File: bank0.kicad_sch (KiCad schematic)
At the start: 2 parts, among them U2 W25Q256FVEI, U201 xc7z010clg400

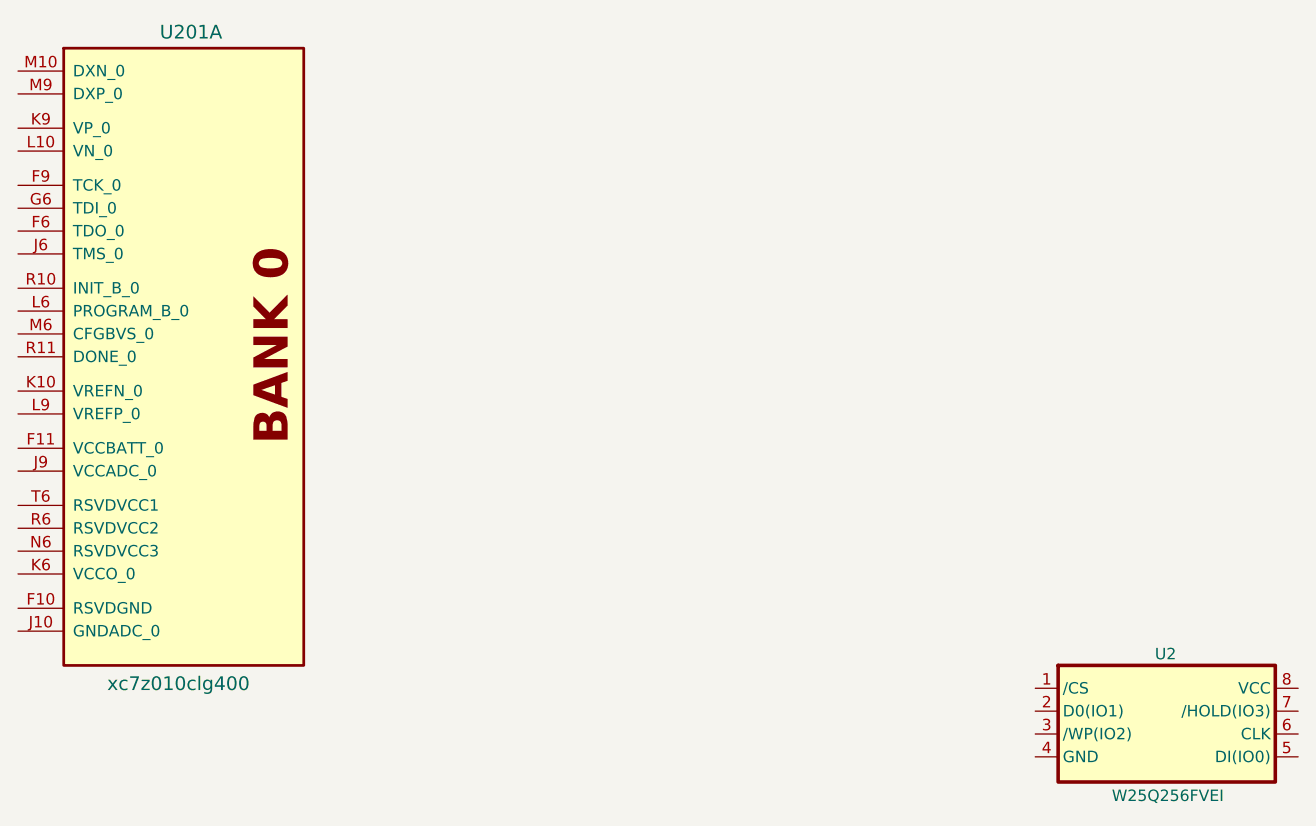
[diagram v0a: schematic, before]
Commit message: feat: finish power sch design
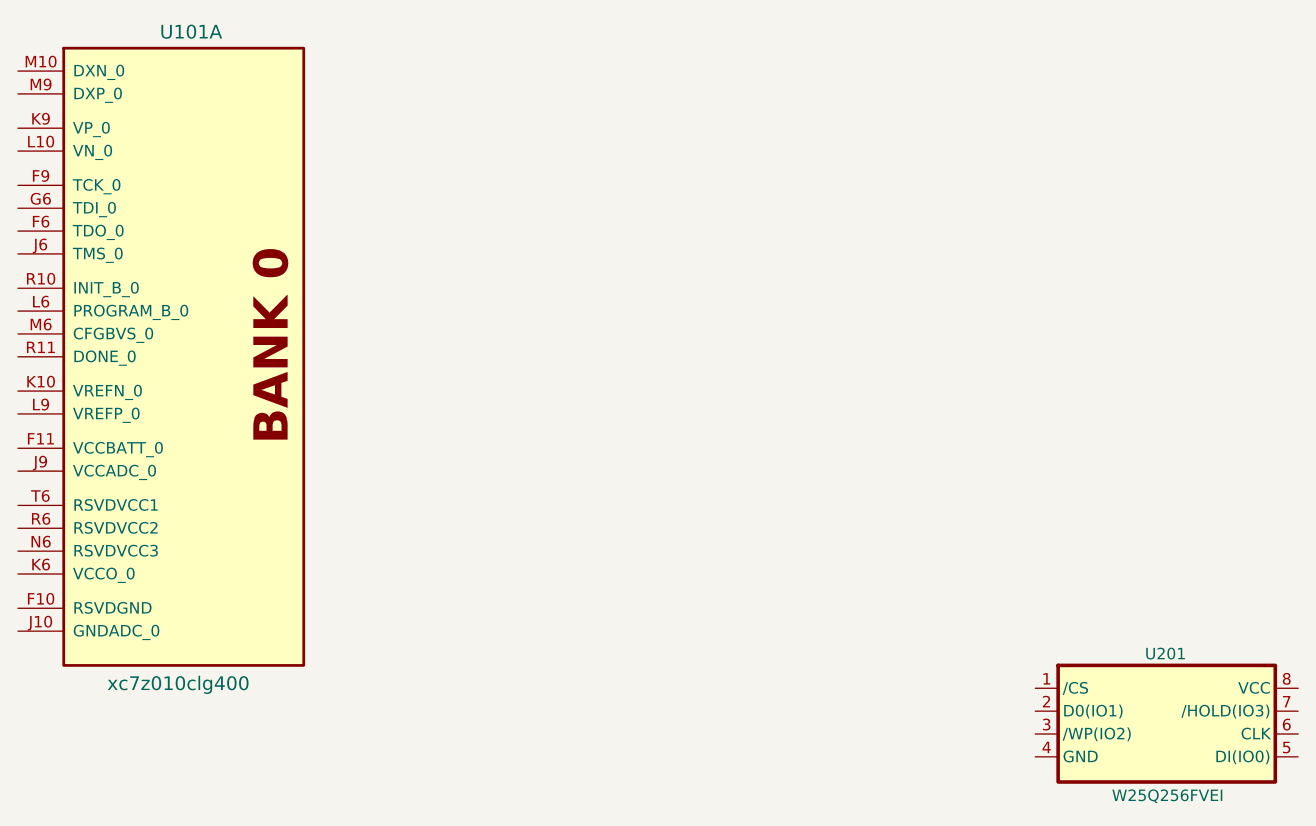
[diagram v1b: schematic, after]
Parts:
- renumbered U201 to U101, U2 to U201
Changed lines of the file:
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@@
 		(in_pos_files yes)
 		(dnp no)
-		(property "Reference" "U201"
+		(property "Reference" "U101"
 			(at 103.378 51.562 0)
 			(show_name no)
@@
 			(project "ZYNQ-SoM"
 				(path "/49bbd0e9-23a3-4368-9660-7ba6c337a59d/2da063c6-0163-4d2d-a242-eeb68f4fd748"
-					(reference "U201")
+					(reference "U101")
 					(unit 1)
 				)
@@
 		(in_pos_files yes)
 		(dnp no)
-		(property "Reference" "U2"
+		(property "Reference" "U201"
 			(at 215.138 120.65 0)
 			(show_name no)
@@
 			(project "ZYNQ-SoM"
 				(path "/49bbd0e9-23a3-4368-9660-7ba6c337a59d/2da063c6-0163-4d2d-a242-eeb68f4fd748"
-					(reference "U2")
+					(reference "U201")
 					(unit 1)
 				)
